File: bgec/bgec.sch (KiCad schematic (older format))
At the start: 3 parts

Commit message: Add the ADCs for the C Stick
I need to figure out how to handle having custom parts; they need to be clonable. Additionally, I probably want to have different schematic sheets for different parts of the thing, like a sheet for powering/grounding everything, a sheet for handling the joysticks+triggers and their ADCs, a sheet for handling the FPGA connections, etc. I definitely need to watch a KiCad tutorial.
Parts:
- added CStickXADC, CStickYADC: TLV571IDW, SOIC127P1030X265-24N, symbol LibraryLoader:TLV571IDW
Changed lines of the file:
@@
 L LibraryLoader:TLV571IDW JoystickYADC
 U 1 1 5E535E80
-P 3500 3000
-F 0 "JoystickYADC" H 4250 3265 50  0000 C CNN
-F 1 "TLV571IDW" H 4250 3174 50  0000 C CNN
-F 2 "SOIC127P1030X265-24N" H 4850 3100 50  0001 L CNN
-F 3 "http://www.ti.com/lit/ds/symlink/tlv571.pdf" H 4850 3000 50  0001 L CNN
-F 4 "8-Bit, 1.25 MSPS Single Ch., Hardware Config., Low Power w/Auto or S/W PowerDown" H 4850 2900 50  0001 L CNN "Description"
-F 5 "2.65" H 4850 2800 50  0001 L CNN "Height"
-F 6 "595-TLV571IDW" H 4850 2700 50  0001 L CNN "Mouser Part Number"
-F 7 "https://www.mouser.com/Search/Refine.aspx?Keyword=595-TLV571IDW" H 4850 2600 50  0001 L CNN "Mouser Price/Stock"
-F 8 "Texas Instruments" H 4850 2500 50  0001 L CNN "Manufacturer_Name"
-F 9 "TLV571IDW" H 4850 2400 50  0001 L CNN "Manufacturer_Part_Number"
-	1    3500 3000
+P 3500 2500
+F 0 "JoystickYADC" H 4250 2765 50  0000 C CNN
+F 1 "TLV571IDW" H 4250 2674 50  0000 C CNN
+F 2 "SOIC127P1030X265-24N" H 4850 2600 50  0001 L CNN
+F 3 "http://www.ti.com/lit/ds/symlink/tlv571.pdf" H 4850 2500 50  0001 L CNN
+F 4 "8-Bit, 1.25 MSPS Single Ch., Hardware Config., Low Power w/Auto or S/W PowerDown" H 4850 2400 50  0001 L CNN "Description"
+F 5 "2.65" H 4850 2300 50  0001 L CNN "Height"
+F 6 "595-TLV571IDW" H 4850 2200 50  0001 L CNN "Mouser Part Number"
+F 7 "https://www.mouser.com/Search/Refine.aspx?Keyword=595-TLV571IDW" H 4850 2100 50  0001 L CNN "Mouser Price/Stock"
+F 8 "Texas Instruments" H 4850 2000 50  0001 L CNN "Manufacturer_Name"
+F 9 "TLV571IDW" H 4850 1900 50  0001 L CNN "Manufacturer_Part_Number"
+	1    3500 2500
 	1    0    0    -1
 $EndComp
+$Comp
+L LibraryLoader:TLV571IDW CStickXADC
+U 1 1 5E53DDAB
+P 3500 4000
+F 0 "CStickXADC" H 4250 4265 50  0000 C CNN
+F 1 "TLV571IDW" H 4250 4174 50  0000 C CNN
+F 2 "SOIC127P1030X265-24N" H 4850 4100 50  0001 L CNN
+F 3 "http://www.ti.com/lit/ds/symlink/tlv571.pdf" H 4850 4000 50  0001 L CNN
+F 4 "8-Bit, 1.25 MSPS Single Ch., Hardware Config., Low Power w/Auto or S/W PowerDown" H 4850 3900 50  0001 L CNN "Description"
+F 5 "2.65" H 4850 3800 50  0001 L CNN "Height"
+F 6 "595-TLV571IDW" H 4850 3700 50  0001 L CNN "Mouser Part Number"
+F 7 "https://www.mouser.com/Search/Refine.aspx?Keyword=595-TLV571IDW" H 4850 3600 50  0001 L CNN "Mouser Price/Stock"
+F 8 "Texas Instruments" H 4850 3500 50  0001 L CNN "Manufacturer_Name"
+F 9 "TLV571IDW" H 4850 3400 50  0001 L CNN "Manufacturer_Part_Number"
+	1    3500 4000
+	1    0    0    -1
+$EndComp
+$Comp
+L LibraryLoader:TLV571IDW CStickYADC
+U 1 1 5E53DDB7
+P 3500 5500
+F 0 "CStickYADC" H 4250 5765 50  0000 C CNN
+F 1 "TLV571IDW" H 4250 5674 50  0000 C CNN
+F 2 "SOIC127P1030X265-24N" H 4850 5600 50  0001 L CNN
+F 3 "http://www.ti.com/lit/ds/symlink/tlv571.pdf" H 4850 5500 50  0001 L CNN
+F 4 "8-Bit, 1.25 MSPS Single Ch., Hardware Config., Low Power w/Auto or S/W PowerDown" H 4850 5400 50  0001 L CNN "Description"
+F 5 "2.65" H 4850 5300 50  0001 L CNN "Height"
+F 6 "595-TLV571IDW" H 4850 5200 50  0001 L CNN "Mouser Part Number"
+F 7 "https://www.mouser.com/Search/Refine.aspx?Keyword=595-TLV571IDW" H 4850 5100 50  0001 L CNN "Mouser Price/Stock"
+F 8 "Texas Instruments" H 4850 5000 50  0001 L CNN "Manufacturer_Name"
+F 9 "TLV571IDW" H 4850 4900 50  0001 L CNN "Manufacturer_Part_Number"
+	1    3500 5500
+	1    0    0    -1
+$EndComp

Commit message: Switch to a consistent label style and use better(?) ADCs
Finding the correct parts to do what I want is hard. On one hand, I want to keep the sample rate high in case a newer protocol needs it, but on the other hand I really don't need anything faster than 4kHz.
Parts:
- removed CStickXADC, CStickYADC, JoystickXADC, JoystickYADC: TLV571IDW, SOIC127P1030X265-24N, symbol LibraryLoader:TLV571IDW
- added ADCCStickX, ADCCStickY, ADCJoystickX, ADCJoystickY: AD7822BRUZ, SOP65P640X120-20N, symbol LibraryLoader:AD7822BRUZ
- renumbered iCE40HX to FPGAiCE40HX
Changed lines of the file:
@@
 $EndDescr
 $Comp
-L LibraryLoader:TLV571IDW JoystickXADC
-U 1 1 5E52F1EE
-P 3500 1000
-F 0 "JoystickXADC" H 4250 1265 50  0000 C CNN
-F 1 "TLV571IDW" H 4250 1174 50  0000 C CNN
-F 2 "SOIC127P1030X265-24N" H 4850 1100 50  0001 L CNN
-F 3 "http://www.ti.com/lit/ds/symlink/tlv571.pdf" H 4850 1000 50  0001 L CNN
-F 4 "8-Bit, 1.25 MSPS Single Ch., Hardware Config., Low Power w/Auto or S/W PowerDown" H 4850 900 50  0001 L CNN "Description"
-F 5 "2.65" H 4850 800 50  0001 L CNN "Height"
-F 6 "595-TLV571IDW" H 4850 700 50  0001 L CNN "Mouser Part Number"
-F 7 "https://www.mouser.com/Search/Refine.aspx?Keyword=595-TLV571IDW" H 4850 600 50  0001 L CNN "Mouser Price/Stock"
-F 8 "Texas Instruments" H 4850 500 50  0001 L CNN "Manufacturer_Name"
-F 9 "TLV571IDW" H 4850 400 50  0001 L CNN "Manufacturer_Part_Number"
-	1    3500 1000
-	1    0    0    -1
-$EndComp
-$Comp
-L LibraryLoader:ICE40HX8K-CT256 iCE40HX
+L LibraryLoader:ICE40HX8K-CT256 FPGAiCE40HX
 U 1 1 5E4F6C64
 P 1000 1000
-F 0 "iCE40HX" H 2050 1265 50  0000 C CNN
+F 0 "FPGAiCE40HX" H 2050 1265 50  0000 C CNN
 F 1 "ICE40HX8K-CT256" H 2050 1174 50  0000 C CNN
 F 2 "BGA256C80P16X16_1400X1400X170" H 2950 1100 50  0001 L CNN
@@
 $EndComp
 $Comp
-L LibraryLoader:TLV571IDW JoystickYADC
-U 1 1 5E535E80
+L LibraryLoader:AD7822BRUZ ADCJoystickX
+U 1 1 5E4E3FD4
+P 3500 1000
+F 0 "ADCJoystickX" H 4300 1265 50  0000 C CNN
+F 1 "AD7822BRUZ" H 4300 1174 50  0000 C CNN
+F 2 "SOP65P640X120-20N" H 4950 1100 50  0001 L CNN
+F 3 "https://componentsearchengine.com/Datasheets/1/AD7822BRUZ.pdf" H 4950 1000 50  0001 L CNN
+F 4 "AD7822BRUZ, 8 bit ADC, Parallel, 20-Pin TSSOP" H 4950 900 50  0001 L CNN "Description"
+F 5 "1.2" H 4950 800 50  0001 L CNN "Height"
+F 6 "584-AD7822BRUZ" H 4950 700 50  0001 L CNN "Mouser Part Number"
+F 7 "https://www.mouser.com/Search/Refine.aspx?Keyword=584-AD7822BRUZ" H 4950 600 50  0001 L CNN "Mouser Price/Stock"
+F 8 "Analog Devices" H 4950 500 50  0001 L CNN "Manufacturer_Name"
+F 9 "AD7822BRUZ" H 4950 400 50  0001 L CNN "Manufacturer_Part_Number"
+	1    3500 1000
+	1    0    0    -1
+$EndComp
+$Comp
+L LibraryLoader:AD7822BRUZ ADCJoystickY
+U 1 1 5E4E4DBF
 P 3500 2500
-F 0 "JoystickYADC" H 4250 2765 50  0000 C CNN
-F 1 "TLV571IDW" H 4250 2674 50  0000 C CNN
-F 2 "SOIC127P1030X265-24N" H 4850 2600 50  0001 L CNN
-F 3 "http://www.ti.com/lit/ds/symlink/tlv571.pdf" H 4850 2500 50  0001 L CNN
-F 4 "8-Bit, 1.25 MSPS Single Ch., Hardware Config., Low Power w/Auto or S/W PowerDown" H 4850 2400 50  0001 L CNN "Description"
-F 5 "2.65" H 4850 2300 50  0001 L CNN "Height"
-F 6 "595-TLV571IDW" H 4850 2200 50  0001 L CNN "Mouser Part Number"
-F 7 "https://www.mouser.com/Search/Refine.aspx?Keyword=595-TLV571IDW" H 4850 2100 50  0001 L CNN "Mouser Price/Stock"
-F 8 "Texas Instruments" H 4850 2000 50  0001 L CNN "Manufacturer_Name"
-F 9 "TLV571IDW" H 4850 1900 50  0001 L CNN "Manufacturer_Part_Number"
+F 0 "ADCJoystickY" H 4300 2765 50  0000 C CNN
+F 1 "AD7822BRUZ" H 4300 2674 50  0000 C CNN
+F 2 "SOP65P640X120-20N" H 4950 2600 50  0001 L CNN
+F 3 "https://componentsearchengine.com/Datasheets/1/AD7822BRUZ.pdf" H 4950 2500 50  0001 L CNN
+F 4 "AD7822BRUZ, 8 bit ADC, Parallel, 20-Pin TSSOP" H 4950 2400 50  0001 L CNN "Description"
+F 5 "1.2" H 4950 2300 50  0001 L CNN "Height"
+F 6 "584-AD7822BRUZ" H 4950 2200 50  0001 L CNN "Mouser Part Number"
+F 7 "https://www.mouser.com/Search/Refine.aspx?Keyword=584-AD7822BRUZ" H 4950 2100 50  0001 L CNN "Mouser Price/Stock"
+F 8 "Analog Devices" H 4950 2000 50  0001 L CNN "Manufacturer_Name"
+F 9 "AD7822BRUZ" H 4950 1900 50  0001 L CNN "Manufacturer_Part_Number"
 	1    3500 2500
 	1    0    0    -1
 $EndComp
 $Comp
-L LibraryLoader:TLV571IDW CStickXADC
-U 1 1 5E53DDAB
+L LibraryLoader:AD7822BRUZ ADCCStickX
+U 1 1 5E4E5FF1
 P 3500 4000
-F 0 "CStickXADC" H 4250 4265 50  0000 C CNN
-F 1 "TLV571IDW" H 4250 4174 50  0000 C CNN
-F 2 "SOIC127P1030X265-24N" H 4850 4100 50  0001 L CNN
-F 3 "http://www.ti.com/lit/ds/symlink/tlv571.pdf" H 4850 4000 50  0001 L CNN
-F 4 "8-Bit, 1.25 MSPS Single Ch., Hardware Config., Low Power w/Auto or S/W PowerDown" H 4850 3900 50  0001 L CNN "Description"
-F 5 "2.65" H 4850 3800 50  0001 L CNN "Height"
-F 6 "595-TLV571IDW" H 4850 3700 50  0001 L CNN "Mouser Part Number"
-F 7 "https://www.mouser.com/Search/Refine.aspx?Keyword=595-TLV571IDW" H 4850 3600 50  0001 L CNN "Mouser Price/Stock"
-F 8 "Texas Instruments" H 4850 3500 50  0001 L CNN "Manufacturer_Name"
-F 9 "TLV571IDW" H 4850 3400 50  0001 L CNN "Manufacturer_Part_Number"
+F 0 "ADCCStickX" H 4300 4265 50  0000 C CNN
+F 1 "AD7822BRUZ" H 4300 4174 50  0000 C CNN
+F 2 "SOP65P640X120-20N" H 4950 4100 50  0001 L CNN
+F 3 "https://componentsearchengine.com/Datasheets/1/AD7822BRUZ.pdf" H 4950 4000 50  0001 L CNN
+F 4 "AD7822BRUZ, 8 bit ADC, Parallel, 20-Pin TSSOP" H 4950 3900 50  0001 L CNN "Description"
+F 5 "1.2" H 4950 3800 50  0001 L CNN "Height"
+F 6 "584-AD7822BRUZ" H 4950 3700 50  0001 L CNN "Mouser Part Number"
+F 7 "https://www.mouser.com/Search/Refine.aspx?Keyword=584-AD7822BRUZ" H 4950 3600 50  0001 L CNN "Mouser Price/Stock"
+F 8 "Analog Devices" H 4950 3500 50  0001 L CNN "Manufacturer_Name"
+F 9 "AD7822BRUZ" H 4950 3400 50  0001 L CNN "Manufacturer_Part_Number"
 	1    3500 4000
 	1    0    0    -1
 $EndComp
 $Comp
-L LibraryLoader:TLV571IDW CStickYADC
-U 1 1 5E53DDB7
+L LibraryLoader:AD7822BRUZ ADCCStickY
+U 1 1 5E4E6A54
 P 3500 5500
-F 0 "CStickYADC" H 4250 5765 50  0000 C CNN
-F 1 "TLV571IDW" H 4250 5674 50  0000 C CNN
-F 2 "SOIC127P1030X265-24N" H 4850 5600 50  0001 L CNN
-F 3 "http://www.ti.com/lit/ds/symlink/tlv571.pdf" H 4850 5500 50  0001 L CNN
-F 4 "8-Bit, 1.25 MSPS Single Ch., Hardware Config., Low Power w/Auto or S/W PowerDown" H 4850 5400 50  0001 L CNN "Description"
-F 5 "2.65" H 4850 5300 50  0001 L CNN "Height"
-F 6 "595-TLV571IDW" H 4850 5200 50  0001 L CNN "Mouser Part Number"
-F 7 "https://www.mouser.com/Search/Refine.aspx?Keyword=595-TLV571IDW" H 4850 5100 50  0001 L CNN "Mouser Price/Stock"
-F 8 "Texas Instruments" H 4850 5000 50  0001 L CNN "Manufacturer_Name"
-F 9 "TLV571IDW" H 4850 4900 50  0001 L CNN "Manufacturer_Part_Number"
+F 0 "ADCCStickY" H 4300 5765 50  0000 C CNN
+F 1 "AD7822BRUZ" H 4300 5674 50  0000 C CNN
+F 2 "SOP65P640X120-20N" H 4950 5600 50  0001 L CNN
+F 3 "https://componentsearchengine.com/Datasheets/1/AD7822BRUZ.pdf" H 4950 5500 50  0001 L CNN
+F 4 "AD7822BRUZ, 8 bit ADC, Parallel, 20-Pin TSSOP" H 4950 5400 50  0001 L CNN "Description"
+F 5 "1.2" H 4950 5300 50  0001 L CNN "Height"
+F 6 "584-AD7822BRUZ" H 4950 5200 50  0001 L CNN "Mouser Part Number"
+F 7 "https://www.mouser.com/Search/Refine.aspx?Keyword=584-AD7822BRUZ" H 4950 5100 50  0001 L CNN "Mouser Price/Stock"
+F 8 "Analog Devices" H 4950 5000 50  0001 L CNN "Manufacturer_Name"
+F 9 "AD7822BRUZ" H 4950 4900 50  0001 L CNN "Manufacturer_Part_Number"
 	1    3500 5500
 	1    0    0    -1

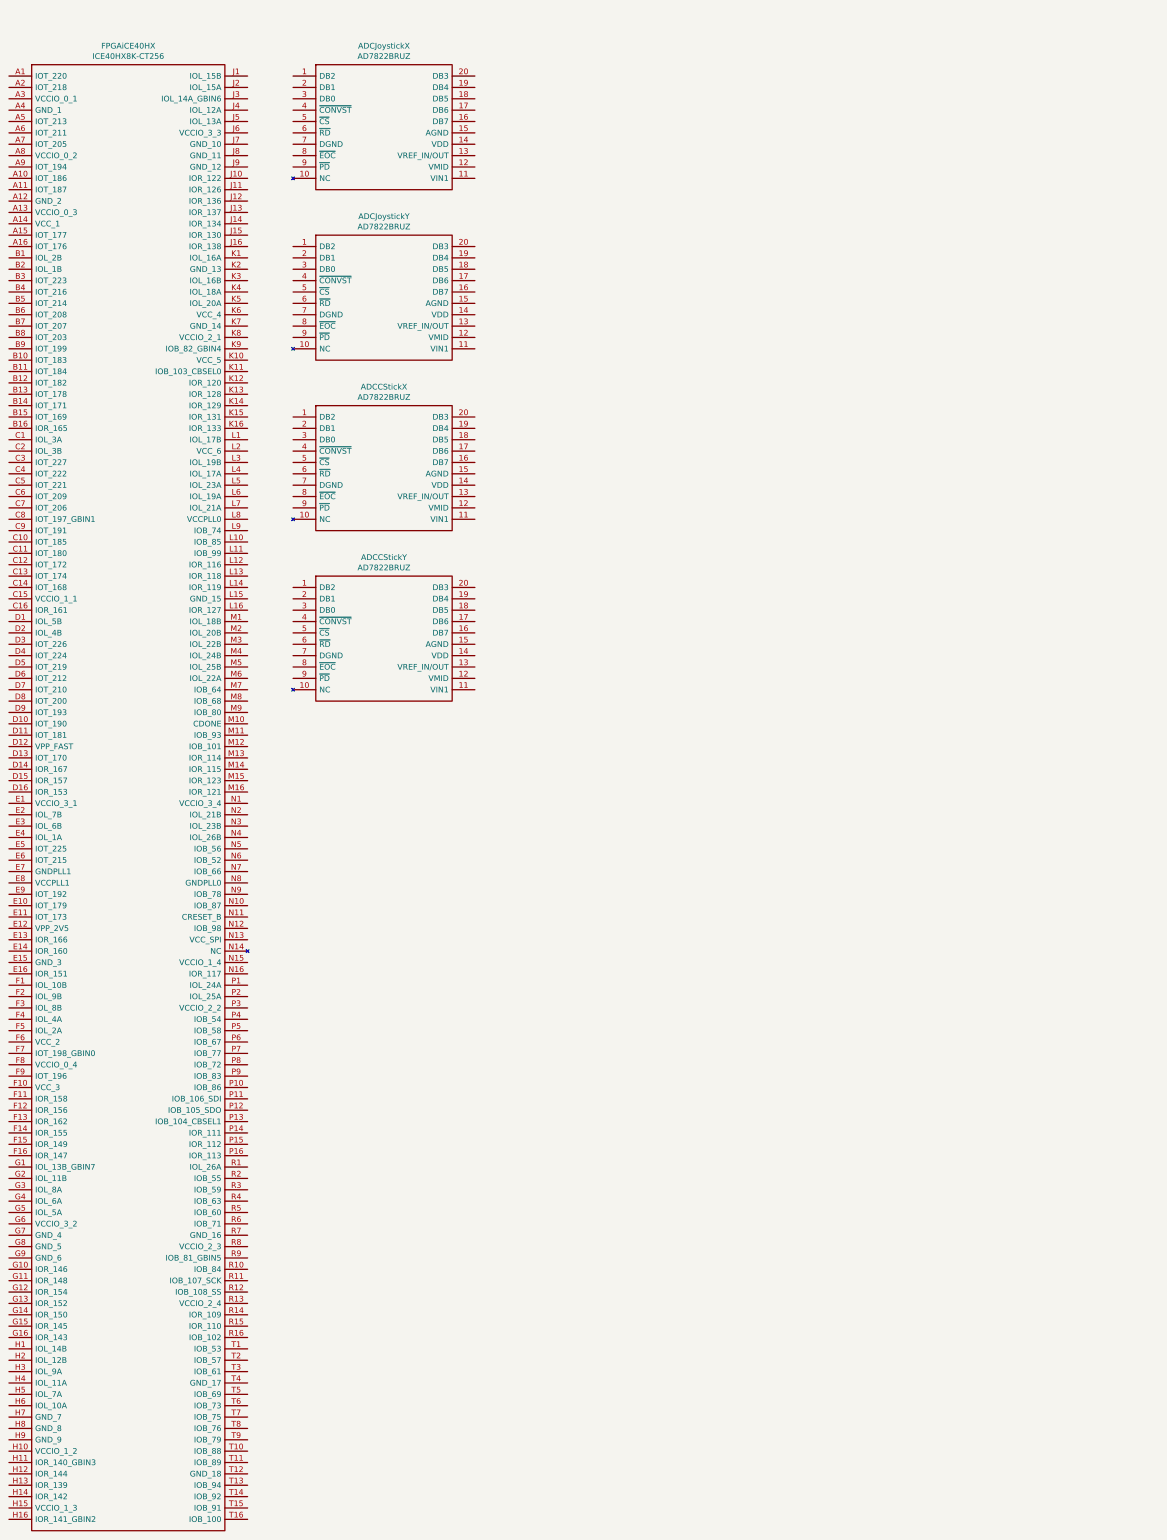
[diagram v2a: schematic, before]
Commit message: Start work on splitting and moving external parts to internal lib
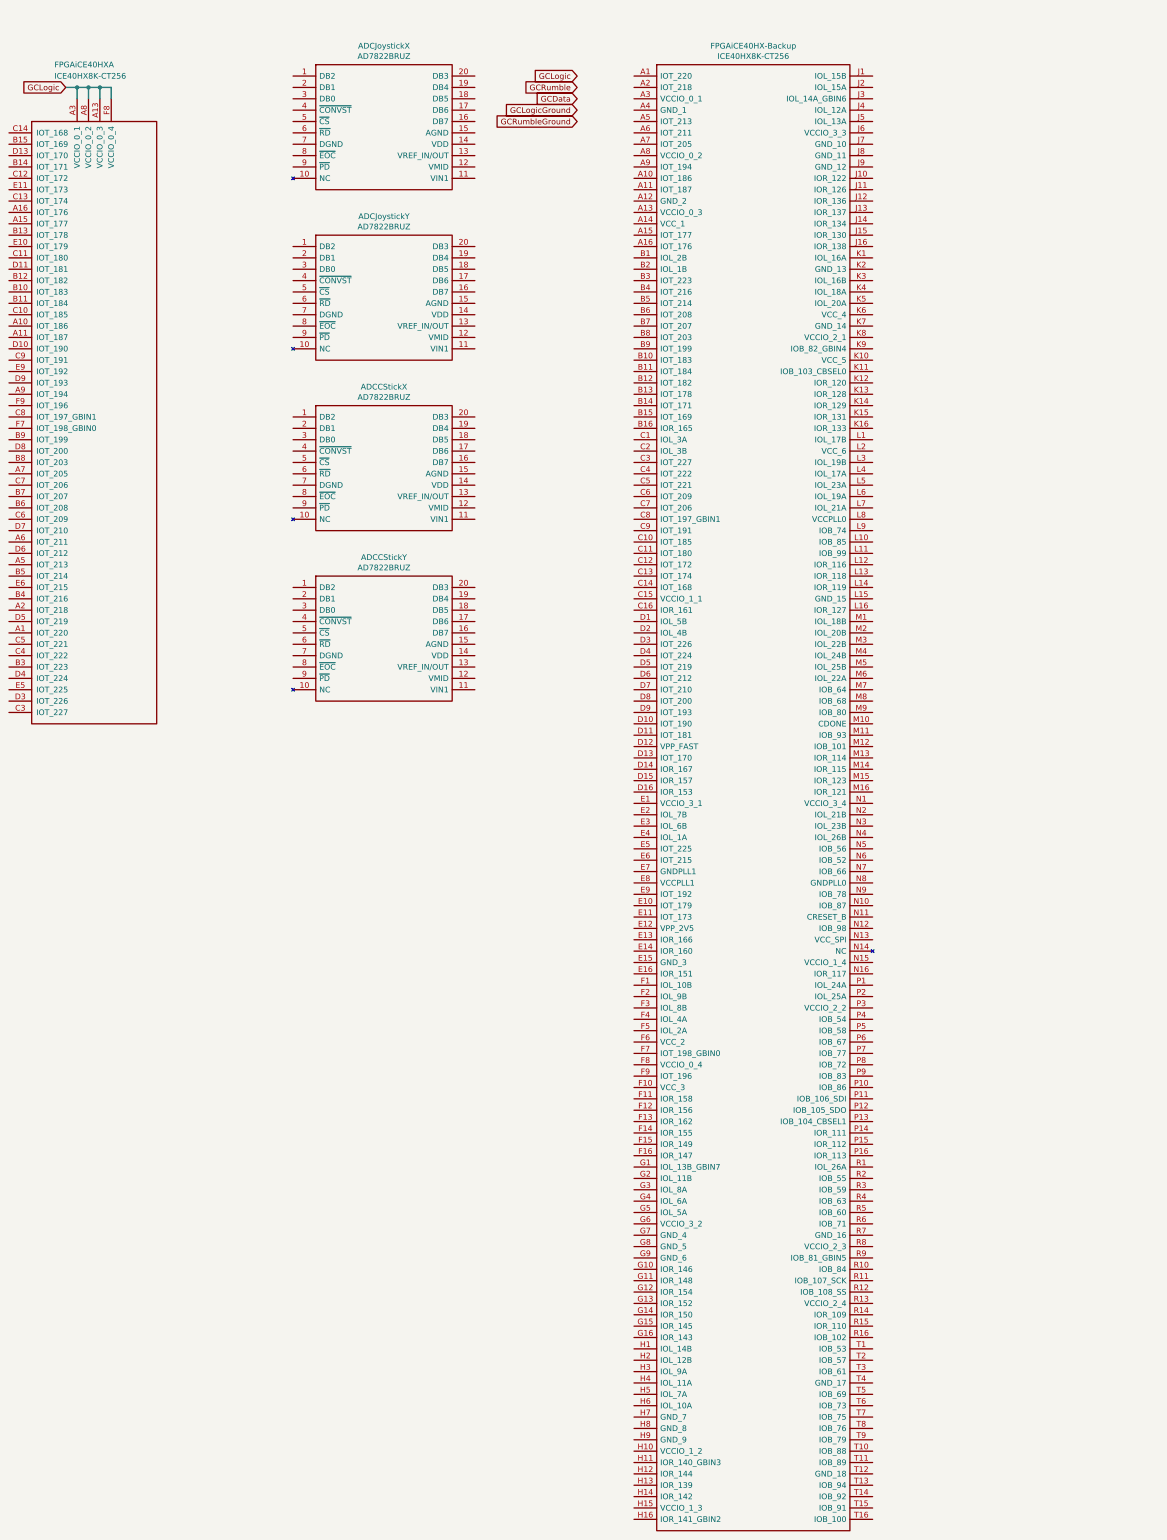
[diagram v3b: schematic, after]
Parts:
- added FPGAiCE40HX: ICE40HX8K-CT256, LibraryLoader:BGA256C80P16X16_1400X1400X170, symbol bgec-components:ICE40HX8K-CT256
- renumbered FPGAiCE40HX to FPGAiCE40HX-Backup
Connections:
- new net GCLogic: FPGAiCE40HX.A13 (VCCIO_0_3), FPGAiCE40HX.A3 (VCCIO_0_1), FPGAiCE40HX.A8 (VCCIO_0_2), FPGAiCE40HX.F8 (VCCIO_0_4)
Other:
- moved on the sheet: FPGAiCE40HX-Backup
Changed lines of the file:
@@
 $EndDescr
-$Comp
-L LibraryLoader:ICE40HX8K-CT256 FPGAiCE40HX
-U 1 1 5E4F6C64
-P 1000 1000
-F 0 "FPGAiCE40HX" H 2050 1265 50  0000 C CNN
-F 1 "ICE40HX8K-CT256" H 2050 1174 50  0000 C CNN
-F 2 "BGA256C80P16X16_1400X1400X170" H 2950 1100 50  0001 L CNN
-F 3 "https://componentsearchengine.com/Datasheets/1/iCE40HX8K-CT256.pdf" H 2950 1000 50  0001 L CNN
-F 4 "FPGA iCE40 HX Family 7680 Cells 40nm Technology 1.2V 256-Pin CSBGA" H 2950 900 50  0001 L CNN "Description"
-F 5 "1.7" H 2950 800 50  0001 L CNN "Height"
-F 6 "842-ICE40HX8K-CT256" H 2950 700 50  0001 L CNN "Mouser Part Number"
-F 7 "https://www.mouser.com/Search/Refine.aspx?Keyword=842-ICE40HX8K-CT256" H 2950 600 50  0001 L CNN "Mouser Price/Stock"
-F 8 "Lattice Semiconductor" H 2950 500 50  0001 L CNN "Manufacturer_Name"
-F 9 "ICE40HX8K-CT256" H 2950 400 50  0001 L CNN "Manufacturer_Part_Number"
-	1    1000 1000
-	1    0    0    -1
-$EndComp
 $Comp
 L LibraryLoader:AD7822BRUZ ADCJoystickX
@@
 	1    0    0    -1
 $EndComp
+Text GLabel 6000 1000 0    50   Input ~ 0
+GCLogic
+Text GLabel 6000 1100 0    50   Input ~ 0
+GCRumble
+Text GLabel 6000 1200 0    50   Input ~ 0
+GCData
+Text GLabel 6000 1300 0    50   Input ~ 0
+GCLogicGround
+Text GLabel 6000 1400 0    50   Input ~ 0
+GCRumbleGround
+$Comp
+L LibraryLoader:ICE40HX8K-CT256 FPGAiCE40HX-Backup
+U 1 1 5E4F6C64
+P 6500 1000
+F 0 "FPGAiCE40HX-Backup" H 7550 1265 50  0000 C CNN
+F 1 "ICE40HX8K-CT256" H 7550 1174 50  0000 C CNN
+F 2 "BGA256C80P16X16_1400X1400X170" H 8450 1100 50  0001 L CNN
+F 3 "https://componentsearchengine.com/Datasheets/1/iCE40HX8K-CT256.pdf" H 8450 1000 50  0001 L CNN
+F 4 "FPGA iCE40 HX Family 7680 Cells 40nm Technology 1.2V 256-Pin CSBGA" H 8450 900 50  0001 L CNN "Description"
+F 5 "1.7" H 8450 800 50  0001 L CNN "Height"
+F 6 "842-ICE40HX8K-CT256" H 8450 700 50  0001 L CNN "Mouser Part Number"
+F 7 "https://www.mouser.com/Search/Refine.aspx?Keyword=842-ICE40HX8K-CT256" H 8450 600 50  0001 L CNN "Mouser Price/Stock"
+F 8 "Lattice Semiconductor" H 8450 500 50  0001 L CNN "Manufacturer_Name"
+F 9 "ICE40HX8K-CT256" H 8450 400 50  0001 L CNN "Manufacturer_Part_Number"
+	1    6500 1000
+	1    0    0    -1
+$EndComp
+$Comp
+L bgec-components:ICE40HX8K-CT256 FPGAiCE40HX
+U 1 1 5E50B913
+P 1000 1500
+F 0 "FPGAiCE40HX" H 1400 2100 50  0000 L CNN
+F 1 "ICE40HX8K-CT256" H 1400 2000 50  0000 L CNN
+F 2 "LibraryLoader:BGA256C80P16X16_1400X1400X170" H 1750 2250 50  0001 C CNN
+F 3 "http://www.latticesemi.com/Products/FPGAandCPLD/iCE40" H 1750 2250 50  0001 C CNN
+	1    1000 1500
+	1    0    0    -1
+$EndComp
+Text GLabel 1500 1100 0    50   Input ~ 0
+GCLogic
+Wire Wire Line
+	1500 1100 1600 1100
+Wire Wire Line
+	1600 1100 1600 1200
+Wire Wire Line
+	1600 1100 1700 1100
+Wire Wire Line
+	1700 1100 1700 1200
+Connection ~ 1600 1100
+Wire Wire Line
+	1700 1100 1800 1100
+Wire Wire Line
+	1800 1100 1800 1200
+Connection ~ 1700 1100
+Wire Wire Line
+	1800 1100 1900 1100
+Wire Wire Line
+	1900 1100 1900 1200
+Connection ~ 1800 1100
 $EndSCHEMATC
